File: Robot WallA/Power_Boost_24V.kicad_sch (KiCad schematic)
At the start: 33 parts, among them IC7 ABXS005A4X341-SRZ, Q2 BSS138, U2 125700D00000G, U3 125700D00000G

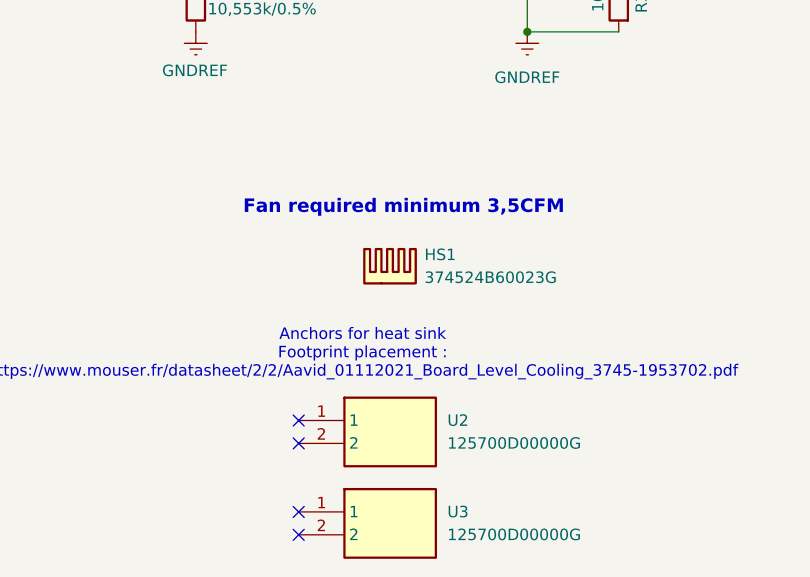
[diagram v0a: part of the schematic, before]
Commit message: Added Thermal pads for heatsinks in BOM.
Updated fab files
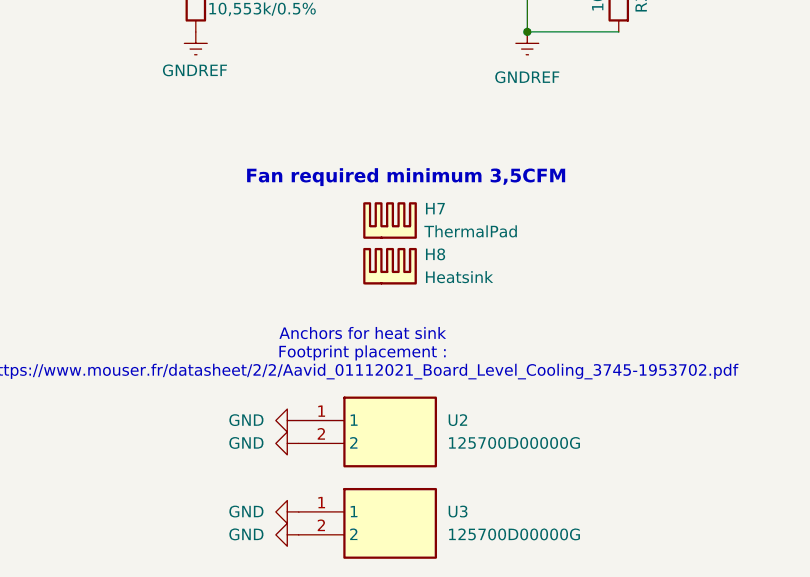
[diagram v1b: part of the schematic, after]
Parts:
- added H7: ThermalPad, symbol Mechanical:Heatsink
- H8: renamed from HS1; value 374524B60023G -> Heatsink
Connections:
- net GND: now also U2.1, U2.2, U3.1, U3.2
- no-connect marks 6 -> 2

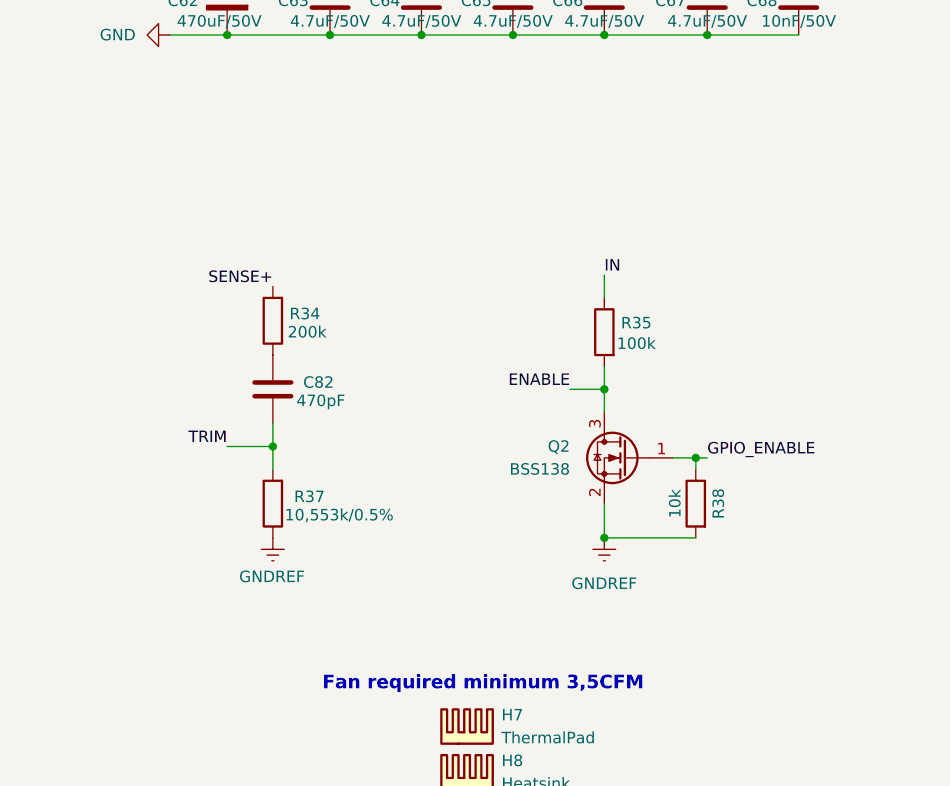
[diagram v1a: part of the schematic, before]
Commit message: Added a trim to 24V in case of (defaulty unplaced)
Updated fab files
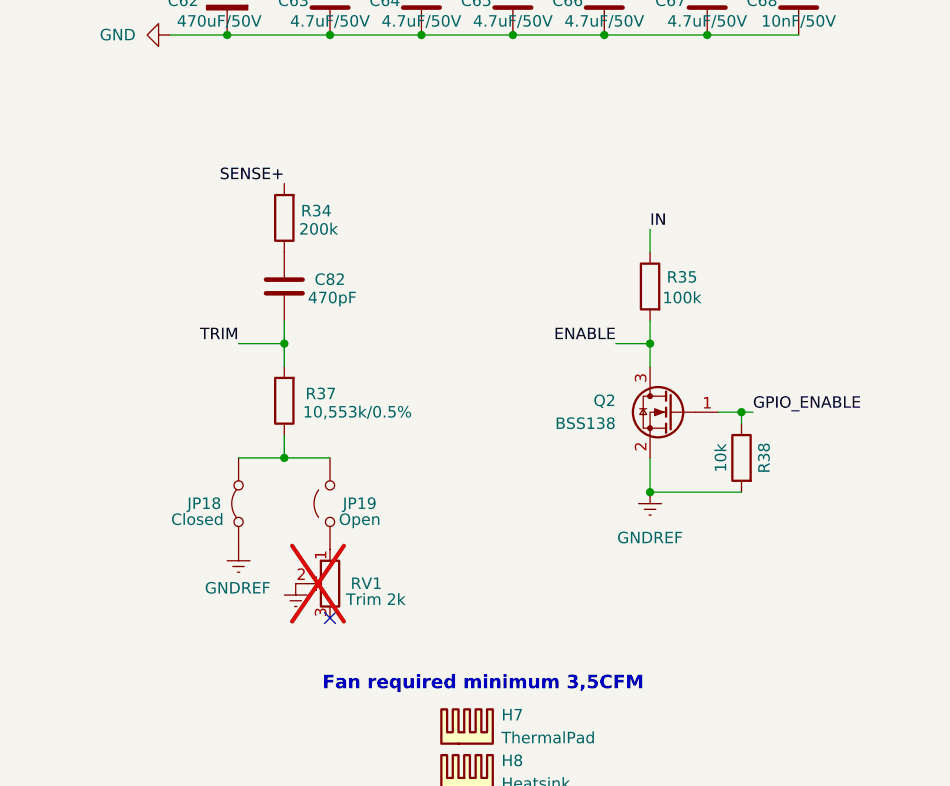
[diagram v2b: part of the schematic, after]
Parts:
- added JP18: Closed, Jumper:SolderJumper-2_P1.3mm_Bridged_RoundedPad1.0x1.5mm, symbol Jumper:Jumper_2_Bridged
- added JP19: Open, Jumper:SolderJumper-2_P1.3mm_Open_RoundedPad1.0x1.5mm, symbol Jumper:Jumper_2_Open
- added RV1: Trim 2k, SamacSys_Parts:TC42X2202E, symbol Device:R_Potentiometer_Trim
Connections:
- net GND: now also JP18.1 (A), RV1.2; no longer R37.1
- new net: JP19.2 (B), RV1.1
- new net: JP18.2 (B), JP19.1 (A), R37.1
- no-connect marks 2 -> 3
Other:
- moved on the sheet: C82, Q2, R34, R35, R37, R38
